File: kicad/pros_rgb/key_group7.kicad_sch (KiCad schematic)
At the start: 16 parts

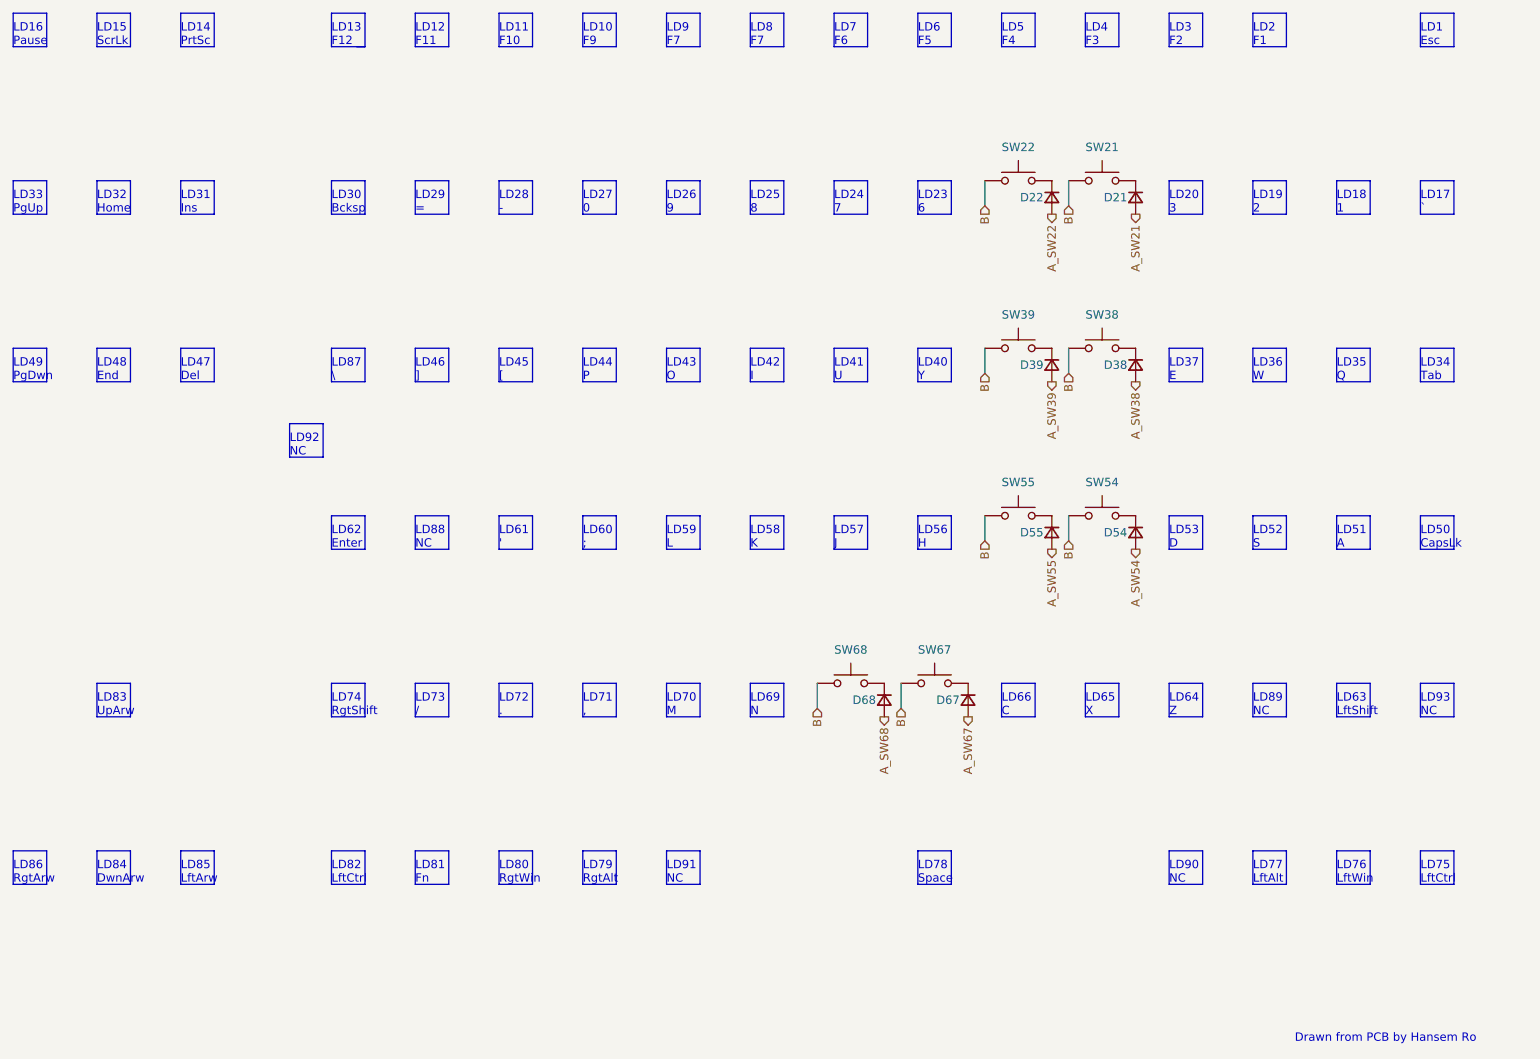
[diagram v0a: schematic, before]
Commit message: kicad/pros_rgb: update key groupings
These new groupings are based off ordering in firmware:
https://github.com/hansemro/pok3r_re_firmware/blob/4b68aa4baf7d28dc8dbf8eebcb1fdb59e7bcd629/disassemble/cmprosrgb/v122/cmprosrgb_v122.txt#L14599-L14629
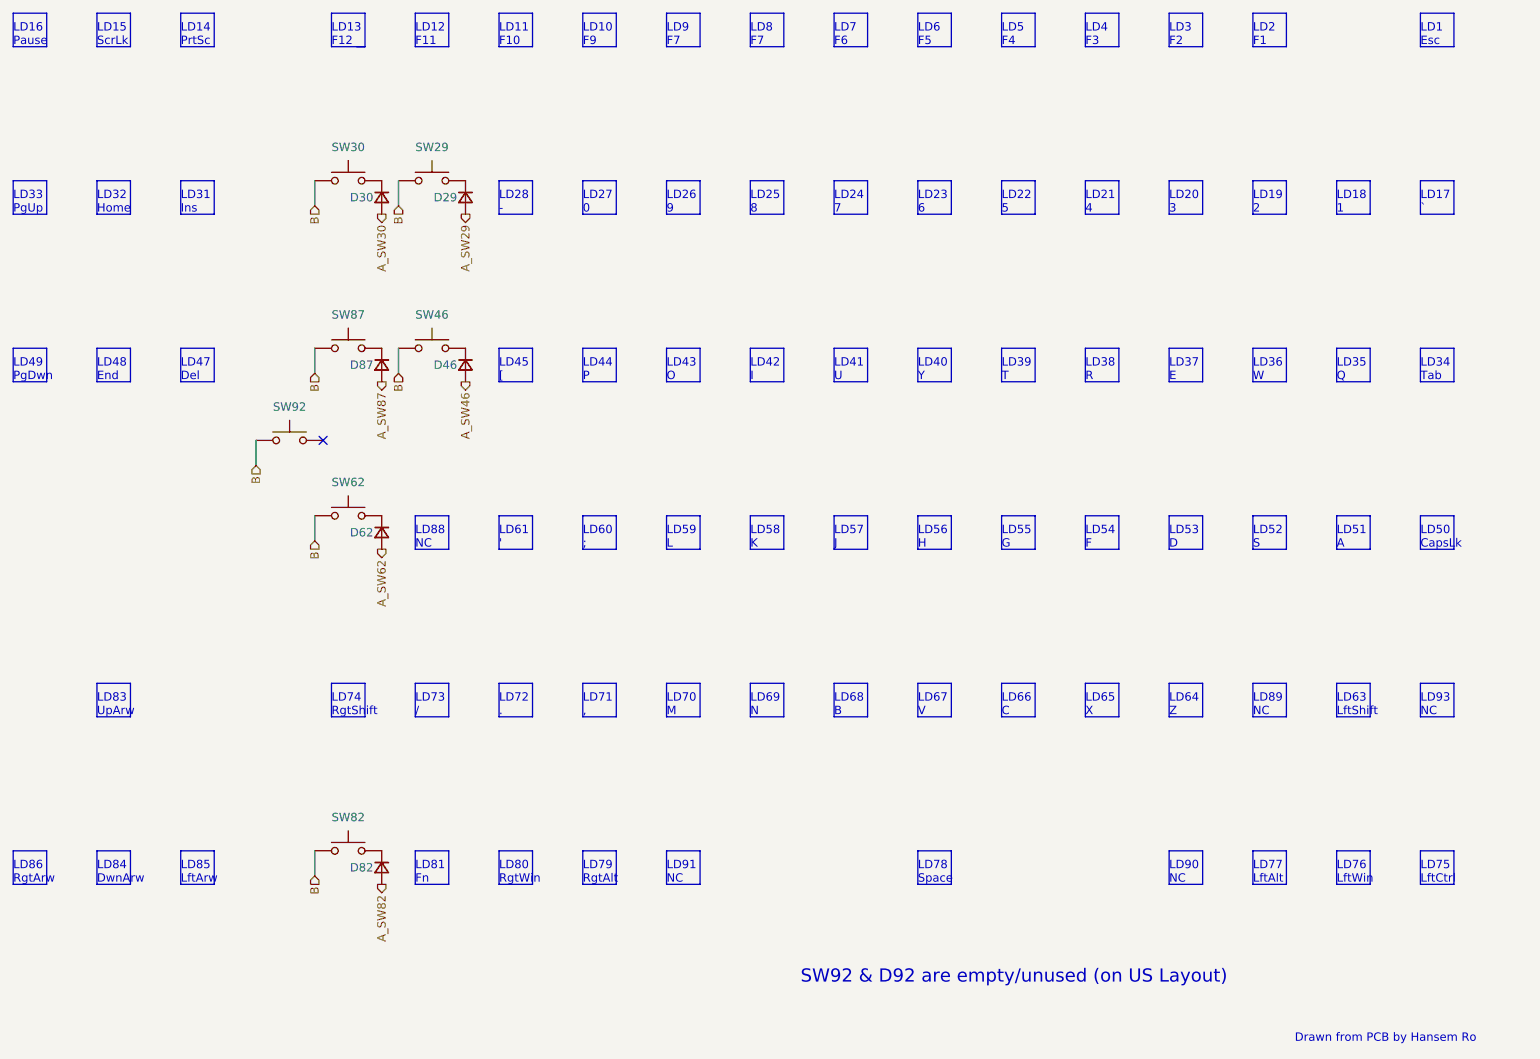
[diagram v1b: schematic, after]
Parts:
- removed D21, D22, D38, D39, D54, D55, D67, D68: ~, symbol Device:D_Small
- removed SW21, SW22, SW38, SW39, SW54, SW55, SW67, SW68: ~, symbol Switch:SW_Push
- added D29, D30, D46, D62, D82, D87: (no value), symbol Device:D_Small
- added SW29, SW30, SW46, SW62, SW82, SW87, SW92: (no value), symbol Switch:SW_Push
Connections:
- net B: now also SW29.1, SW30.1, SW46.1, SW62.1, SW82.1, SW87.1, SW92.1
- new net: D87.1 (K), SW87.2
- new net: D82.1 (K), SW82.2
- new net: D46.1 (K), SW46.2
- new net: D29.1 (K), SW29.2
- new net: D30.1 (K), SW30.2
- new net: D62.1 (K), SW62.2
- new net A_SW29: D29.2 (A)
- new net A_SW30: D30.2 (A)
- new net A_SW46: D46.2 (A)
- new net A_SW62: D62.2 (A)
- new net A_SW82: D82.2 (A)
- new net A_SW87: D87.2 (A)
- no-connect marks 0 -> 1
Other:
- note added: "LD21 4"
- note added: "LD22 5"
- note added: "LD38 R"
- note added: "LD39 T"
- note added: "LD54 F"
- note added: "LD55 G"
- note added: "LD67 V"
- note added: "LD68 B"
- note added: "SW92 & D92 are empty/unused (on US Layout)"
- note removed: "LD29 ="
- note removed: "LD30 Bcksp"
- note removed: "LD46 ]"
- note removed: "LD62 Enter"
- note removed: "LD82 LftCtrl"
- note removed: "LD87 \"
- note removed: "LD92 NC"

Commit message: kicad/pros_rgb: mark as Rev. B
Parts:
- D29, D30, D46, D62, D82, D87, SW29, SW30, SW46, SW62, SW82, SW87, SW92: value (none) -> ~
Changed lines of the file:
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@@
     (in_bom yes) (on_board yes)
     (property "Reference" "SW87" (id 0) (at 109.22 69.85 0))
-    (property "Value" "" (id 1) (at 109.22 69.85 0))
+    (property "Value" "~" (id 1) (at 109.22 69.85 0))
     (property "Footprint" "" (id 2) (at 109.22 69.85 0)
       (effects (font (size 1.27 1.27)) hide)
@@
     (in_bom yes) (on_board yes)
     (property "Reference" "SW82" (id 0) (at 109.22 146.05 0))
-    (property "Value" "" (id 1) (at 109.22 146.05 0))
+    (property "Value" "~" (id 1) (at 109.22 146.05 0))
     (property "Footprint" "" (id 2) (at 109.22 146.05 0)
       (effects (font (size 1.27 1.27)) hide)
@@
     (in_bom yes) (on_board yes)
     (property "Reference" "SW46" (id 0) (at 121.92 69.85 0))
-    (property "Value" "" (id 1) (at 121.92 69.85 0))
+    (property "Value" "~" (id 1) (at 121.92 69.85 0))
     (property "Footprint" "" (id 2) (at 121.92 69.85 0)
       (effects (font (size 1.27 1.27)) hide)
@@
       (effects (font (size 1.27 1.27)) (justify right))
     )
-    (property "Value" "" (id 1) (at 129.54 78.7399 90)
+    (property "Value" "~" (id 1) (at 129.54 78.7399 90)
       (effects (font (size 1.27 1.27)) (justify left))
     )
@@
       (effects (font (size 1.27 1.27)) (justify right))
     )
-    (property "Value" "" (id 1) (at 116.84 154.9399 90)
+    (property "Value" "~" (id 1) (at 116.84 154.9399 90)
       (effects (font (size 1.27 1.27)) (justify left))
     )
@@
       (effects (font (size 1.27 1.27)) (justify right))
     )
-    (property "Value" "" (id 1) (at 129.54 53.3399 90)
+    (property "Value" "~" (id 1) (at 129.54 53.3399 90)
       (effects (font (size 1.27 1.27)) (justify left))
     )
@@
       (effects (font (size 1.27 1.27)) (justify right))
     )
-    (property "Value" "" (id 1) (at 116.84 78.7399 90)
+    (property "Value" "~" (id 1) (at 116.84 78.7399 90)
       (effects (font (size 1.27 1.27)) (justify left))
     )
@@
       (effects (font (size 1.27 1.27)) (justify right))
     )
-    (property "Value" "" (id 1) (at 116.84 53.3399 90)
+    (property "Value" "~" (id 1) (at 116.84 53.3399 90)
       (effects (font (size 1.27 1.27)) (justify left))
     )
@@
     (in_bom yes) (on_board yes)
     (property "Reference" "SW29" (id 0) (at 121.92 44.45 0))
-    (property "Value" "" (id 1) (at 121.92 44.45 0))
+    (property "Value" "~" (id 1) (at 121.92 44.45 0))
     (property "Footprint" "" (id 2) (at 121.92 44.45 0)
       (effects (font (size 1.27 1.27)) hide)
@@
       (effects (font (size 1.27 1.27)) (justify right))
     )
-    (property "Value" "" (id 1) (at 116.84 104.1399 90)
+    (property "Value" "~" (id 1) (at 116.84 104.1399 90)
       (effects (font (size 1.27 1.27)) (justify left))
     )
@@
     (in_bom yes) (on_board yes)
     (property "Reference" "SW30" (id 0) (at 109.22 44.45 0))
-    (property "Value" "" (id 1) (at 109.22 44.45 0))
+    (property "Value" "~" (id 1) (at 109.22 44.45 0))
     (property "Footprint" "" (id 2) (at 109.22 44.45 0)
       (effects (font (size 1.27 1.27)) hide)
@@
     (in_bom yes) (on_board yes)
     (property "Reference" "SW62" (id 0) (at 109.22 95.25 0))
-    (property "Value" "" (id 1) (at 109.22 95.25 0))
+    (property "Value" "~" (id 1) (at 109.22 95.25 0))
     (property "Footprint" "" (id 2) (at 109.22 95.25 0)
       (effects (font (size 1.27 1.27)) hide)
@@
     (in_bom yes) (on_board yes)
     (property "Reference" "SW92" (id 0) (at 100.33 83.82 0))
-    (property "Value" "" (id 1) (at 100.33 83.82 0))
+    (property "Value" "~" (id 1) (at 100.33 83.82 0))
     (property "Footprint" "" (id 2) (at 100.33 83.82 0)
       (effects (font (size 1.27 1.27)) hide)

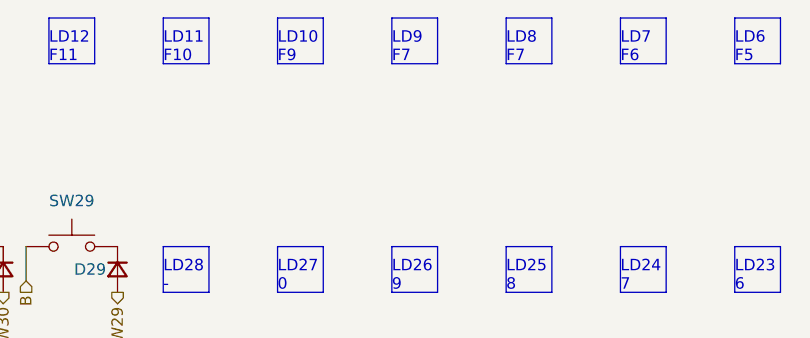
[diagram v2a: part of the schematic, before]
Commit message: kicad/pros_rgb: fix typos
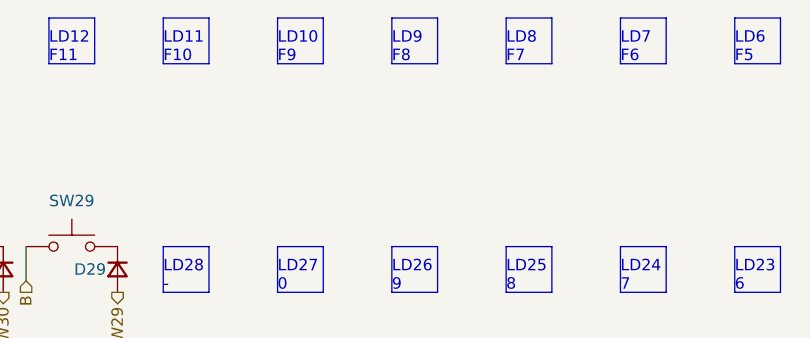
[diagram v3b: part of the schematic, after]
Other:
- note added: "LD9 F8"
- note removed: "LD9 F7"
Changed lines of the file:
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@@
     (effects (font (size 1.27 1.27)) (justify left bottom))
   )
-  (text "LD9\nF7" (at 157.48 29.21 0)
+  (text "LD9\nF8" (at 157.48 29.21 0)
     (effects (font (size 1.27 1.27)) (justify left bottom))
   )
